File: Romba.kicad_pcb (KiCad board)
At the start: 2 copper layers, 1 part, among them U1 ESP32-DEVKITC-32D

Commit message: Holy Headache added most footprints
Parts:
- added 12V_Bulk_Capacitor1: ~1000 microFarads, Capacitor_THT:CP_Radial_D8.0mm_P3.50mm, F.Cu at (133.3, 75.7)
- added 12V_Ceramic_Capacitor1: .1 microFarads, Capacitor_SMD:C_0805_2012Metric, F.Cu at (127.8, 72.5)
- added 5V_Bulk_Capacitor1: ~470 microFarads, Capacitor_THT:CP_Radial_D6.3mm_P2.50mm, F.Cu at (133.0, 44.0)
- added 5V_Ceramic_Capacitor1: .1 microFarads, Capacitor_SMD:C_0805_2012Metric, F.Cu at (127.8, 75.5)
- added 5V_Ceramic_Capacitor2: .1 microFarads, Capacitor_SMD:C_0805_2012Metric, F.Cu at (127.8, 78.5)
- added 5V_Ceramic_Capacitor3: .1 microFarads, Capacitor_SMD:C_0805_2012Metric, F.Cu at (127.8, 81.5)
- added 5V_Ceramic_Capacitor4: .1 microFarads, Capacitor_SMD:C_0805_2012Metric, F.Cu at (116.5, 98.0)
- added FB1: FerriteBead, Resistor_SMD:R_1206_3216Metric, F.Cu at (149.0, 45.0)
- added FB2: FerriteBead, Resistor_SMD:R_1206_3216Metric, F.Cu at (165.0, 42.5)
- added J1: LIDAR UART, Connector_PinHeader_2.54mm:PinHeader_1x06_P2.54mm_Vertical, F.Cu at (151.0, 95.8)
- added J2: Gyro, Connector_PinHeader_2.54mm:PinHeader_1x08_P2.54mm_Vertical, F.Cu at (161.0, 90.7)
- added J3: 5v-Bus, TerminalBlock:TerminalBlock_MaiXu_MX126-5.0-02P_1x02_P5.00mm, F.Cu at (112.0, 45.5)
- added J4: 12V-Bus, TerminalBlock:TerminalBlock_MaiXu_MX126-5.0-02P_1x02_P5.00mm, F.Cu at (105.2, 58.0)
- added MotorL_Bulk_Ceramic1: 47 microFarads, Capacitor_THT:CP_Radial_D5.0mm_P2.00mm, F.Cu at (132.4, 83.8)
- added MotorL_HF_Ceramic1: .1 microFarads, Capacitor_SMD:C_0805_2012Metric, F.Cu at (104.5, 100.0)
- added MotorR_Bulk_Ceramic1: 47 microFarads, Capacitor_THT:CP_Radial_D5.0mm_P2.00mm, F.Cu at (132.4, 90.3)
- added MotorR_HF_Ceramic1: .1 microFarads, Capacitor_SMD:C_0805_2012Metric, F.Cu at (121.5, 110.0)
- added UMotor_L1: DRV8871DDA, Connector_PinHeader_2.54mm:PinHeader_1x04_P2.54mm_Vertical, F.Cu at (144.0, 58.0)
- added UMotor_L2POWER1: DRV8871DDA, TerminalBlock:TerminalBlock_MaiXu_MX126-5.0-02P_1x02_P5.00mm, F.Cu at (80.2, 70.5)
- added UMotor_R1: DRV8871DDA, Connector_PinHeader_2.54mm:PinHeader_1x04_P2.54mm_Vertical, F.Cu at (164.5, 60.5)
- added UMotor_R2POWER1: DRV8871DDA, TerminalBlock:TerminalBlock_MaiXu_MX126-5.0-02P_1x02_P5.00mm, F.Cu at (79.0, 104.0)
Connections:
- U1 pad J2-1: unconnected-(U1-3V3-PadJ2-1) -> +3.3V
- U1 pad J2-10: unconnected-(U1-IO26-PadJ2-10) -> /PWM2_L
- U1 pad J2-11: unconnected-(U1-IO27-PadJ2-11) -> /PWM1_R
- U1 pad J2-12: unconnected-(U1-IO14-PadJ2-12) -> /PWM2_R
- U1 pad J2-14: unconnected-(U1-GND1-PadJ2-14) -> GND
- U1 pad J2-19: unconnected-(U1-EXT_5V-PadJ2-19) -> +5V
- U1 pad J2-5: unconnected-(U1-IO34-PadJ2-5) -> /EncoderB_L
- U1 pad J2-6: unconnected-(U1-IO35-PadJ2-6) -> /EncoderA_R
- U1 pad J2-7: unconnected-(U1-IO32-PadJ2-7) -> /EncoderB_L
- U1 pad J2-8: unconnected-(U1-IO33-PadJ2-8) -> /EncoderA_L
- U1 pad J2-9: unconnected-(U1-IO25-PadJ2-9) -> /PWM1_L
- U1 pad J3-1: unconnected-(U1-GND3-PadJ3-1) -> GND
- U1 pad J3-11: unconnected-(U1-IO17-PadJ3-11) -> /LiDAR_RXD/SDA
- U1 pad J3-12: unconnected-(U1-IO16-PadJ3-12) -> /LiDAR_TXD\SCL
- U1 pad J3-3: unconnected-(U1-IO22-PadJ3-3) -> /Gyro_SCL\Rx
- U1 pad J3-6: unconnected-(U1-IO21-PadJ3-6) -> /Gyro_SDA\Tx
- U1 pad J3-7: unconnected-(U1-GND2-PadJ3-7) -> GND

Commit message: chickenmcnegus
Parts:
- added J5: Motor_L, Connector_PinHeader_2.54mm:PinHeader_1x06_P2.54mm_Horizontal, F.Cu at (49.5, 84.6)
- added J6: Motor_R, Connector_PinHeader_2.54mm:PinHeader_1x06_P2.54mm_Horizontal, F.Cu at (49.5, 101.1)
- UMotor_L2POWER1, UMotor_R2POWER1: footprint TerminalBlock:TerminalBlock_MaiXu_MX126-5.0-02P_1x02_P5.00mm -> Connector_PinHeader_2.54mm:PinHeader_1x02_P2.54mm_Vertical
- moved U1 136.8 mm to (79.3, 83.5)
- moved FB2 125.5 mm to (70.0, 124.5), turned to 90 degrees
- moved UMotor_R1 112.3 mm to (59.0, 98.8), turned to 180 degrees
- moved FB1 109.3 mm to (74.0, 124.5), turned to 90 degrees
- moved 12V_Bulk_Capacitor1 97.0 mm to (50.0, 125.5)
- moved 5V_Bulk_Capacitor1 91.7 mm to (90.0, 125.0)
- moved UMotor_L1 89.2 mm to (59.0, 85.1), turned to 180 degrees
- moved J3 86.6 mm to (78.8, 125.5)
- moved MotorR_Bulk_Ceramic1 81.0 mm to (53.0, 106.0)
- moved J4 80.8 mm to (60.8, 125.5)
- moved MotorL_Bulk_Ceramic1 80.7 mm to (53.0, 69.5)
- moved 12V_Ceramic_Capacitor1 78.7 mm to (63.0, 117.0)
- moved 5V_Ceramic_Capacitor3 68.3 mm to (67.3, 113.0)
- moved J2 67.3 mm to (99.0, 64.6)
- moved MotorR_HF_Ceramic1 59.1 mm to (62.5, 106.0), turned to 90 degrees
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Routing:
- net +3.3V: track 0.00 -> 32.9 mm
- net GND: vias 0 -> 9
- added copper zone on B.Cu, net GND
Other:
- board outline added: 85 x 85.5 mm

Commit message: Work done on PCB Traces
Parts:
- moved 5V_Ceramic_Capacitor2 1.40 mm to (103.0, 90.5), turned to -90 degrees
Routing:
- net +12V: track 0.00 -> 96.4 mm
- net GND: track 0.00 -> 86.6 mm, vias 9 -> 10
- net +5V: track 0.00 -> 41.7 mm
- net /12V_Bus: track 0.00 -> 31.2 mm
- net /5V_Bus: track 0.00 -> 26.9 mm
- net /ML-: track 0.00 -> 14.6 mm
- net /ML+: track 0.00 -> 11.8 mm
- net /PWM2_L: track 0.00 -> 9.27 mm
- net /PWM1_L: track 0.00 -> 9.27 mm
- net /Gyro_SDA\Tx: track 0.00 -> 8.74 mm
- net /Gyro_SCL\Rx: track 0.00 -> 7.36 mm
- net +3.3V: track 32.9 -> 39.6 mm

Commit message: please be all gone
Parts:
- removed 12V_Bulk_Capacitor1: ~1000 microFarads, Capacitor_THT:CP_Radial_D8.0mm_P3.50mm
- removed 12V_Ceramic_Capacitor1, 5V_Ceramic_Capacitor1, 5V_Ceramic_Capacitor2, 5V_Ceramic_Capacitor3, 5V_Ceramic_Capacitor4, MotorL_HF_Ceramic1, MotorR_HF_Ceramic1: .1 microFarads, Capacitor_SMD:C_0805_2012Metric
- removed 5V_Bulk_Capacitor1: ~470 microFarads, Capacitor_THT:CP_Radial_D6.3mm_P2.50mm
- removed FB1, FB2: FerriteBead, Resistor_SMD:R_1206_3216Metric
- removed J1: LIDAR UART, Connector_PinHeader_2.54mm:PinHeader_1x06_P2.54mm_Vertical
- removed J2: Gyro, Connector_PinHeader_2.54mm:PinHeader_1x08_P2.54mm_Vertical
- removed J3: 5v-Bus, TerminalBlock:TerminalBlock_MaiXu_MX126-5.0-02P_1x02_P5.00mm
- removed J4: 12V-Bus, TerminalBlock:TerminalBlock_MaiXu_MX126-5.0-02P_1x02_P5.00mm
- removed J5: Motor_L, Connector_PinHeader_2.54mm:PinHeader_1x06_P2.54mm_Horizontal
- removed J6: Motor_R, Connector_PinHeader_2.54mm:PinHeader_1x06_P2.54mm_Horizontal
- removed MotorL_Bulk_Ceramic1, MotorR_Bulk_Ceramic1: 47 microFarads, Capacitor_THT:CP_Radial_D5.0mm_P2.00mm
- removed U1: ESP32-DEVKITC-32D, Amazon ESP32:MODULE_ESP32-DEVKITC-32D
- removed UMotor_L1, UMotor_R1: DRV8871DDA, Connector_PinHeader_2.54mm:PinHeader_1x04_P2.54mm_Vertical
- removed UMotor_L2POWER1, UMotor_R2POWER1: DRV8871DDA, Connector_PinHeader_2.54mm:PinHeader_1x02_P2.54mm_Vertical
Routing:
- net +12V: track 96.4 -> 0.00 mm
- net GND: track 86.6 -> 0.00 mm, vias 10 -> 0
- net +5V: track 41.7 -> 0.00 mm
- net +3.3V: track 39.6 -> 0.00 mm
- net /12V_Bus: track 31.2 -> 0.00 mm
- net /5V_Bus: track 26.9 -> 0.00 mm
- net /ML-: track 14.6 -> 0.00 mm
- net /ML+: track 11.8 -> 0.00 mm
- net /PWM2_L: track 9.27 -> 0.00 mm
- net /PWM1_L: track 9.27 -> 0.00 mm
- net /Gyro_SDA\Tx: track 8.74 -> 0.00 mm
- net /Gyro_SCL\Rx: track 7.36 -> 0.00 mm
- removed copper zone on B.Cu, net GND
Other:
- board outline removed

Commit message: a bit lost
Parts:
- added 12V_Bulk_Capacitor1: ~1000 microFarads, Capacitor_THT:CP_Radial_D8.0mm_P3.50mm, F.Cu at (138.4, 82.9)
- added 12V_Ceramic_Capacitor1: .1 microFarads, Capacitor_SMD:C_0805_2012Metric, F.Cu at (132.9, 79.6)
- added 5V_Bulk_Capacitor1: ~470 microFarads, Capacitor_THT:CP_Radial_D6.3mm_P2.50mm, F.Cu at (138.5, 71.9)
- added 5V_Ceramic_Capacitor1: .1 microFarads, Capacitor_SMD:C_0805_2012Metric, F.Cu at (132.9, 82.6)
- added 5V_Ceramic_Capacitor2: .1 microFarads, Capacitor_SMD:C_0805_2012Metric, F.Cu at (132.9, 85.7)
- added 5V_Ceramic_Capacitor3: .1 microFarads, Capacitor_SMD:C_0805_2012Metric, F.Cu at (132.9, 88.7)
- added 5V_Ceramic_Capacitor4: .1 microFarads, Capacitor_SMD:C_0805_2012Metric, F.Cu at (132.9, 91.7)
- added FB1: FerriteBead, Resistor_SMD:R_1206_3216Metric, F.Cu at (119.7, 92.0)
- added FB2: FerriteBead, Resistor_SMD:R_1206_3216Metric, F.Cu at (119.7, 95.3)
- added J1: LIDAR UART, Connector_PinHeader_2.54mm:PinHeader_1x06_P2.54mm_Vertical, F.Cu at (133.4, 63.1)
- added J2: Gyro, Connector_PinHeader_2.54mm:PinHeader_1x08_P2.54mm_Vertical, F.Cu at (128.4, 80.4)
- added J3: 5v-Bus, TerminalBlock:TerminalBlock_MaiXu_MX126-5.0-02P_1x02_P5.00mm, F.Cu at (108.4, 83.2)
- added J4: 12V-Bus, TerminalBlock:TerminalBlock_MaiXu_MX126-5.0-02P_1x02_P5.00mm, F.Cu at (108.4, 93.3)
- added J5: Motor_L, Connector_PinHeader_2.54mm:PinHeader_1x06_P2.54mm_Horizontal, F.Cu at (106.7, 63.1)
- added J6: Motor_R, Connector_PinHeader_2.54mm:PinHeader_1x06_P2.54mm_Horizontal, F.Cu at (120.0, 63.1)
- added MotorL_Bulk_Ceramic1: 47 microFarads, Capacitor_THT:CP_Radial_D5.0mm_P2.00mm, F.Cu at (137.5, 91.0)
- added MotorL_HF_Ceramic1: .1 microFarads, Capacitor_SMD:C_0805_2012Metric, F.Cu at (132.9, 94.7)
- added MotorR_Bulk_Ceramic1: 47 microFarads, Capacitor_THT:CP_Radial_D5.0mm_P2.00mm, F.Cu at (137.5, 97.5)
- added MotorR_HF_Ceramic1: .1 microFarads, Capacitor_SMD:C_0805_2012Metric, F.Cu at (132.9, 97.7)
- added UMotor_L1: DRV8871DDA, Connector_PinHeader_2.54mm:PinHeader_1x04_P2.54mm_Vertical, F.Cu at (119.2, 80.4)
- added UMotor_L2POWER1: DRV8871DDA, Connector_PinHeader_2.54mm:PinHeader_1x02_P2.54mm_Vertical, F.Cu at (138.0, 63.1)
- added UMotor_R1: DRV8871DDA, Connector_PinHeader_2.54mm:PinHeader_1x04_P2.54mm_Vertical, F.Cu at (123.8, 80.4)
- added UMotor_R2POWER1: DRV8871DDA, Connector_PinHeader_2.54mm:PinHeader_1x02_P2.54mm_Vertical, F.Cu at (142.6, 63.1)

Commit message: Fixed library issue good to start routing
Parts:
- added U1: ESP32-DEVKITC-32D, Amazon ESP32:MODULE_ESP32-DEVKITC-32D, F.Cu at (170.3, 83.5)

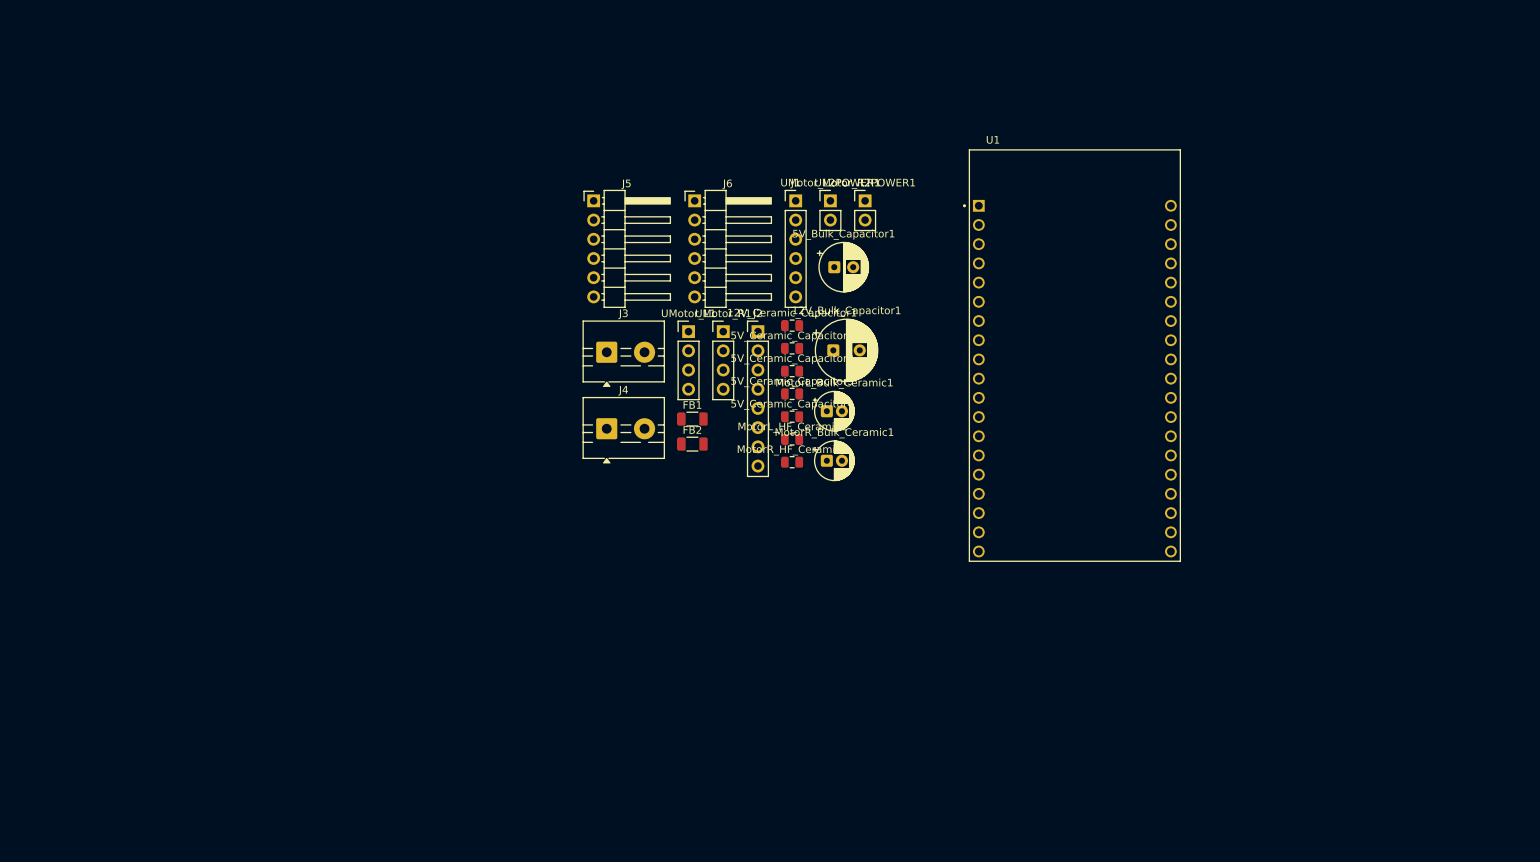
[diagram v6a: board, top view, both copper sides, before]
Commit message: Updated PCB Layout to more optimal state
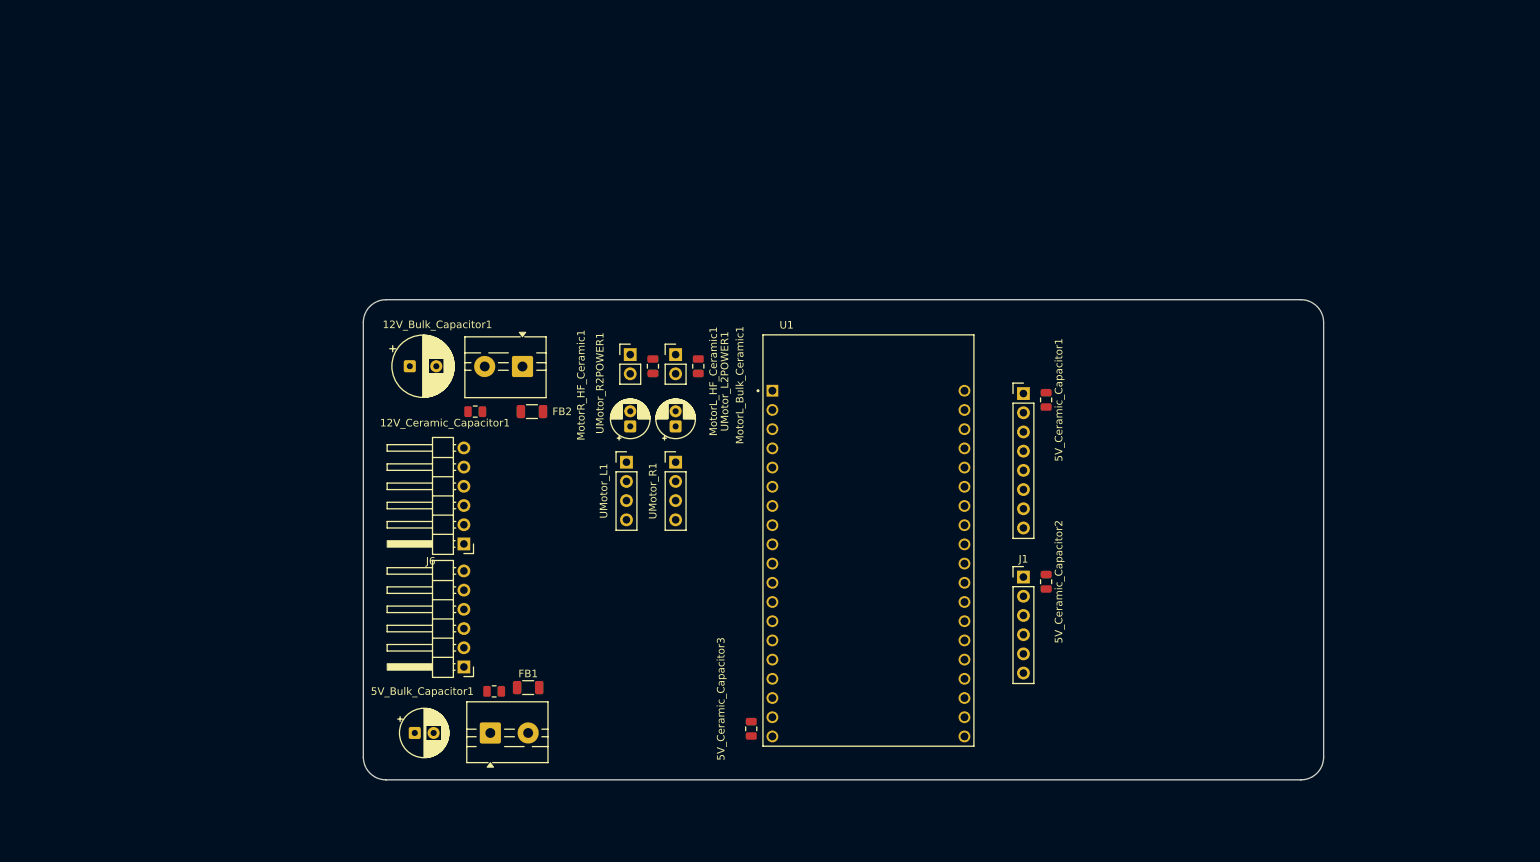
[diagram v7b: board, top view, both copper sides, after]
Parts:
- moved 5V_Bulk_Capacitor1 82.9 mm to (83.0, 133.5)
- moved J5 64.0 mm to (89.5, 124.8), turned to 180 degrees
- moved J1 58.2 mm to (163.5, 112.9)
- moved 12V_Bulk_Capacitor1 56.0 mm to (82.3, 85.0)
- moved J6 54.7 mm to (89.5, 108.5), turned to 180 degrees
- moved 5V_Ceramic_Capacitor4 53.6 mm to (93.5, 128.0)
- moved J3 52.6 mm to (93.0, 133.5)
- moved 5V_Ceramic_Capacitor3 44.6 mm to (127.5, 132.9), turned to 90 degrees
- moved 5V_Ceramic_Capacitor2 43.6 mm to (166.5, 113.5), turned to -90 degrees
- moved 12V_Ceramic_Capacitor1 43.4 mm to (91.0, 91.0), turned to 180 degrees
- moved FB1 41.6 mm to (98.0, 127.5)
- moved UMotor_R2POWER1 37.1 mm to (111.5, 83.5)
- moved U1 36.7 mm to (143.0, 108.0)
- moved J2 36.1 mm to (163.5, 88.6)
- moved 5V_Ceramic_Capacitor1 34.3 mm to (166.5, 89.5), turned to -90 degrees
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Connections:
- UMotor_L1 pad 1: Net-(UMotor_L1-GND-Pad1) -> /PWM1_L
- UMotor_L1 pad 3: /PWM1_L -> /ML+
- UMotor_L1 pad 4: unconnected-(UMotor_L1-ILIM-Pad4) -> /ML-
- UMotor_R1 pad 1: Net-(UMotor_R1-GND-Pad1) -> /PWM1_R
- UMotor_R1 pad 3: /PWM1_R -> /MR+
- UMotor_R1 pad 4: unconnected-(UMotor_R1-ILIM-Pad4) -> /MR-
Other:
- board outline added: 127 x 63.5 mm

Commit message: Finished PCB Routing
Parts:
- moved UMotor_R1 23.6 mm to (94.0, 95.9)
- moved UMotor_L1 21.4 mm to (95.0, 111.9)
- moved 12V_Bulk_Capacitor1 3.81 mm to (86.2, 85.0), turned to 180 degrees
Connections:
- J5 pad 1: /EncoderB_L -> /EncoderA_L
- J5 pad 2: /EncoderA_L -> /EncoderB_L
- J6 pad 1: /EncoderB_L -> /EncoderA_R
- J6 pad 2: /EncoderA_R -> /EncoderB_R
- U1 pad J2-10: /PWM2_L -> /PWM2_R
- U1 pad J2-11: /PWM1_R -> /PWM1_L
- U1 pad J2-12: /PWM2_R -> /PWM2_L
- U1 pad J2-5: /EncoderB_L -> /EncoderB_R
- U1 pad J2-9: /PWM1_L -> /PWM1_R
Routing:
- net +5V: track 0.00 -> 119.9 mm
- net GND: track 0.00 -> 56.5 mm, vias 0 -> 13
- net +12V: track 0.00 -> 52.9 mm
- net /EncoderB_L: track 0.00 -> 48.6 mm
- net /EncoderA_L: track 0.00 -> 48.6 mm
- net /EncoderA_R: track 0.00 -> 43.9 mm
- net /EncoderB_R: track 0.00 -> 43.9 mm
- net /PWM1_R: track 0.00 -> 41.6 mm
- net /PWM2_R: track 0.00 -> 41.6 mm
- net +3.3V: track 0.00 -> 37.0 mm
- net /PWM2_L: track 0.00 -> 36.0 mm
- net /PWM1_L: track 0.00 -> 36.0 mm
- net /12V_Bus: track 0.00 -> 26.8 mm
- net /5V_Bus: track 0.00 -> 24.1 mm
- net /Gyro_SDA\Tx: track 0.00 -> 9.75 mm
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- added copper zone on B.Cu, net GND
